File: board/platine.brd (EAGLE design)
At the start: 100 x 80 mm, 33 parts, among them IC2 SPS-1, T1 BC846, T2 BC846, X11 22-23-2031, X15 22-23-2031, X16 22-23-2031, X17 22-23-2031, X18 22-23-2031, X3 1751251, X4 1751251, X5 1751251, X7 1751248, X8 1751248, X9 1751248

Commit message: New board
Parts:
- added C10, C2, C3, C4, C5, C6, C7, C8, C9: (no value), rcl:C1206
- added L1, L2, L3, L4: (no value), rcl:R0402
- added R8: 220K, rcl:R0603
- C1: device rcl:C1206 -> rcl:C0603
- R1: value 10k -> 1K; device rcl:M1206 -> rcl:R0603
- R2, R3, R5, R6, R7: device rcl:M1206 -> rcl:R0603
- R4: value 3k -> 1K; device rcl:M1206 -> rcl:R0603
- moved X18 34.9 mm to (61.4, 49.2), turned to 90 degrees
- moved R6 32.0 mm to (40.0, 39.1), turned to 180 degrees
- moved R7 30.7 mm to (41.9, 36.6)
- moved SV1 29.2 mm to (40.7, 5.23)
- moved R5 27.9 mm to (39.1, 36.1), turned to 270 degrees
- moved C1 27.3 mm to (31.3, 34.0)
- moved X15 26.3 mm to (52.5, 38.8), turned to 90 degrees
- moved R2 18.9 mm to (35.7, 54.2), turned to 270 degrees
- moved R4 17.7 mm to (41.2, 54.8), turned to 90 degrees
- moved X17 12.9 mm to (52.6, 49.2), turned to 90 degrees
- moved R3 10.8 mm to (36.5, 57.3), turned to 180 degrees
- moved U$1 10.4 mm to (31.6, 43.5), turned to 90 degrees
- moved X16 9.46 mm to (61.4, 38.8), turned to 90 degrees
- moved R1 8.71 mm to (35.7, 60.7), turned to 90 degrees
- moved T2 6.54 mm to (40.2, 60.5)
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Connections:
- removed net N$25: F3.2A, X10.1, X11.1
- new net N$46: L3.1, SV1.21
- new net N$47: L4.2, R6.1, R7.2
- net +24V: now also C4.2, C6.2, C7.2, C9.2
- net +5V: now also C2.2, C5.2, F3.2A, X10.1, X11.1
- net GND: now also C10.1, C2.1, C3.1, C4.1, C5.1, C6.1, C7.1, C8.1, C9.1, R8.1, SV1.14, SV1.20, SV1.25, SV1.6, SV1.9, X11.3, X2.8, X2.9, X3.1, X3.2, X4.2, X4.3, X5.2, X5.3, X7.1, X8.2, X9.2
- net N$22: now also L2.2; no longer SV1.23
- net N$23: now also L3.2; no longer SV1.19
- net N$3: now also R8.2
- net N$41: now also C3.2
- net N$42: now also L1.1, SV1.24; no longer X3.1, X3.2, X4.2, X4.3, X5.2, X5.3
- net N$44: now also C10.2, C8.2, F2.2A, X9.1
- net N$45: now also L2.1, SV1.23; no longer X7.1, X8.2, X9.2
- net N$5: now also L1.2; no longer SV1.5
- net N$6: now also L4.1, SV1.19; no longer R6.1, R7.2, SV1.21
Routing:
- net GND: track 0.00 -> 641.3 mm, vias 0 -> 2
- net +5V: track 0.00 -> 277.5 mm, vias 0 -> 6
- net +24V: track 0.00 -> 247.9 mm, vias 0 -> 3
- net N$30: track 0.00 -> 74.0 mm, vias 0 -> 2
- net N$6: track 0.00 -> 52.6 mm, vias 0 -> 1
- net N$10: track 0.00 -> 52.1 mm, vias 0 -> 1
- net N$39: track 0.00 -> 46.7 mm
- net N$38: track 0.00 -> 46.6 mm
- net N$37: track 0.00 -> 45.6 mm
- net N$44: track 0.00 -> 44.9 mm
- net N$19: track 0.00 -> 44.3 mm
- net N$18: track 0.00 -> 43.5 mm, vias 0 -> 1
- net N$17: track 0.00 -> 41.6 mm, vias 0 -> 1
- net N$28: track 0.00 -> 40.8 mm, vias 0 -> 1
- net N$14: track 0.00 -> 40.3 mm
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- added copper zone on layer 1, net GND
- added copper zone on layer 16, net GND

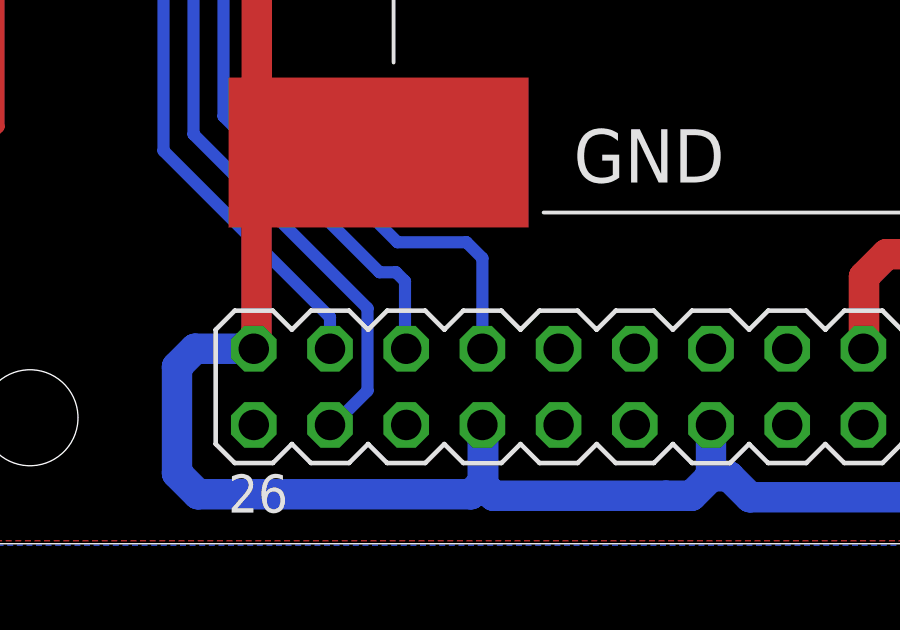
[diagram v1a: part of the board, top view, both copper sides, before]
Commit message: fix(board): switch MISO and MOSI
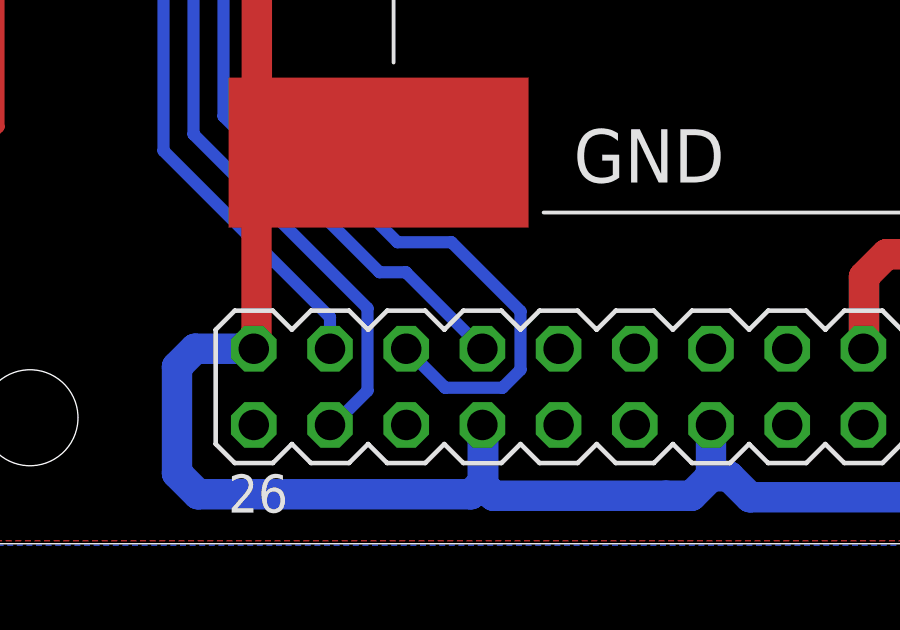
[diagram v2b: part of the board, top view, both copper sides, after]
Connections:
- net N$46: now also SV1.19; no longer SV1.21
- net N$6: now also SV1.21; no longer SV1.19
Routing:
- net N$6: track 52.6 -> 58.1 mm
- net N$46: track 24.4 -> 25.6 mm
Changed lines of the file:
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@@
 <?xml version="1.0" encoding="utf-8"?>
 <!DOCTYPE eagle SYSTEM "eagle.dtd">
-<eagle version="6.3">
+<eagle version="6.4">
 <drawing>
 <settings>
@@
 <signal name="N$6">
 <contactref element="L4" pad="1"/>
-<contactref element="SV1" pad="19"/>
 <wire x1="44.44" y1="34.64" x2="44.83" y2="34.25" width="0.4064" layer="1"/>
 <wire x1="44.83" y1="34.25" x2="46" y2="34.25" width="0.4064" layer="1"/>
@@
 <wire x1="25.6" y1="31.25" x2="25.6" y2="14.7" width="0.4064" layer="16"/>
 <wire x1="25.6" y1="14.7" x2="30.25" y2="10.05" width="0.4064" layer="16"/>
-<wire x1="30.25" y1="10.05" x2="32.55" y2="10.05" width="0.4064" layer="16"/>
-<wire x1="32.55" y1="10.05" x2="33.08" y2="9.52" width="0.4064" layer="16"/>
-<wire x1="33.08" y1="9.52" x2="33.08" y2="6.5" width="0.4064" layer="16"/>
+<contactref element="SV1" pad="21"/>
+<wire x1="32.05" y1="10.05" x2="34.35" y2="7.75" width="0.4064" layer="16"/>
+<wire x1="34.35" y1="7.75" x2="34.35" y2="5.8" width="0.4064" layer="16"/>
+<wire x1="34.35" y1="5.8" x2="33.75" y2="5.2" width="0.4064" layer="16"/>
+<wire x1="33.75" y1="5.2" x2="31.84" y2="5.2" width="0.4064" layer="16"/>
+<wire x1="31.84" y1="5.2" x2="30.54" y2="6.5" width="0.4064" layer="16"/>
+<wire x1="30.25" y1="10.05" x2="32.05" y2="10.05" width="0.4064" layer="16"/>
 </signal>
 <signal name="N$26">
@@
 <signal name="N$46">
 <contactref element="L3" pad="1"/>
-<contactref element="SV1" pad="21"/>
-<wire x1="30.54" y1="6.5" x2="30.5" y2="6.54" width="0.4064" layer="16"/>
-<wire x1="30.5" y1="6.54" x2="30.5" y2="8.75" width="0.4064" layer="16"/>
-<wire x1="30.5" y1="8.75" x2="30.2" y2="9.05" width="0.4064" layer="16"/>
-<wire x1="30.2" y1="9.05" x2="29.65" y2="9.05" width="0.4064" layer="16"/>
+<wire x1="30.53" y1="9.05" x2="29.65" y2="9.05" width="0.4064" layer="16"/>
 <wire x1="29.65" y1="9.05" x2="24.45" y2="14.25" width="0.4064" layer="16"/>
 <wire x1="24.45" y1="14.25" x2="24.45" y2="21.2" width="0.4064" layer="16"/>
@@
 <wire x1="20.25" y1="22.9" x2="20.23" y2="22.92" width="0.4064" layer="1"/>
 <wire x1="20.23" y1="22.92" x2="20.23" y2="24.84" width="0.4064" layer="1"/>
+<contactref element="SV1" pad="19"/>
+<wire x1="30.53" y1="9.05" x2="33.08" y2="6.5" width="0.4064" layer="16"/>
 </signal>
 <signal name="N$47">

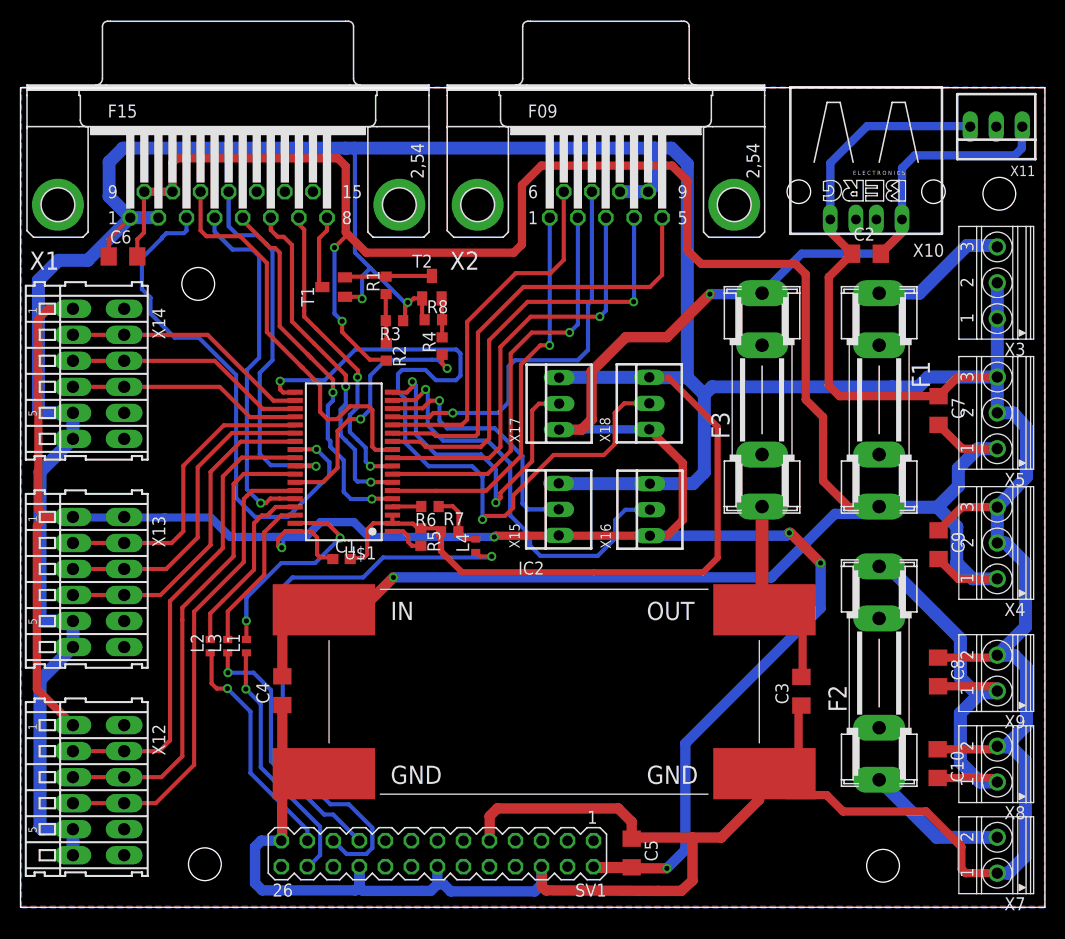
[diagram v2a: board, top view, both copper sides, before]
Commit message: Replaced wrong transistor
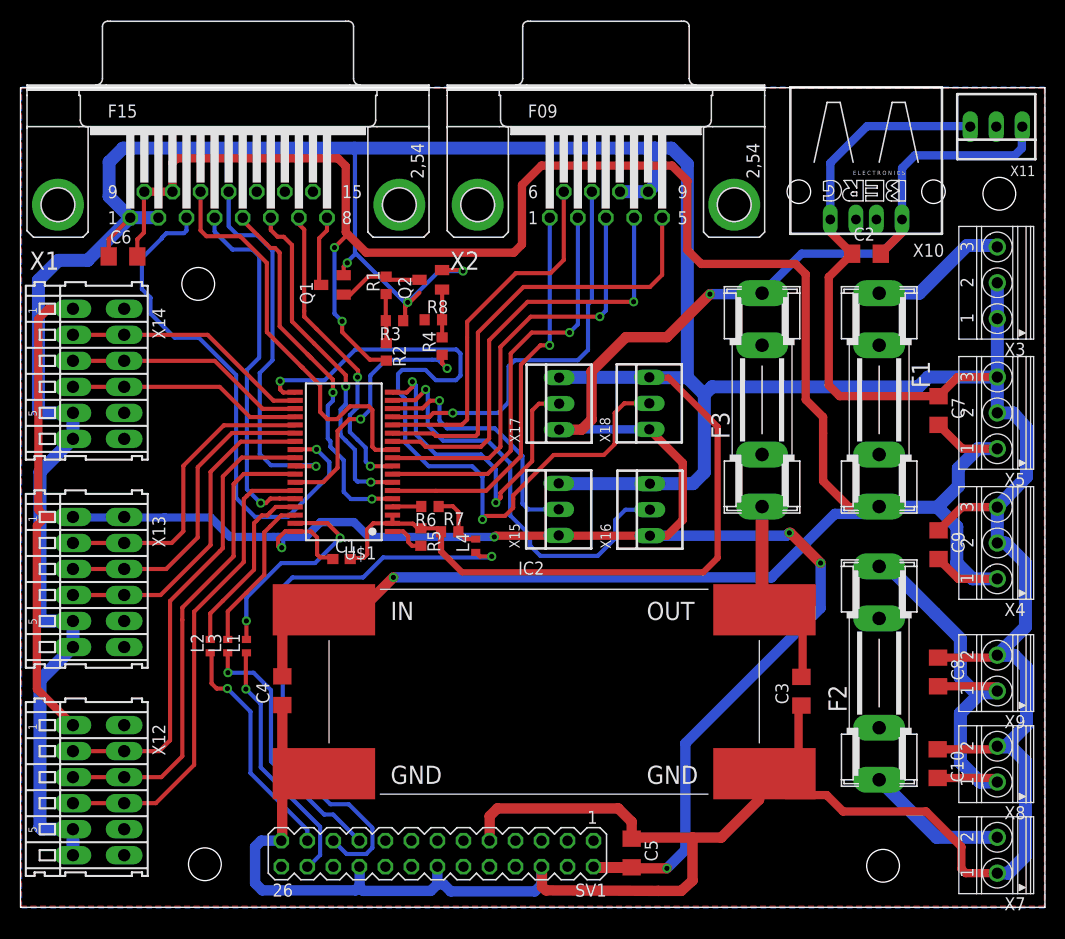
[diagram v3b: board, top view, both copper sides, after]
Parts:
- removed T1, T2: BC846, transistor:SOT23-EBC
- added Q1, Q2: (no value), semicon-smd-ipc:SOT23
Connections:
- net GND: now also Q1.2, Q2.2; no longer T1.E, T2.E
- net N$2: now also Q1.1, Q2.3; no longer T1.B, T2.C
- net N$3: now also Q2.1; no longer T2.B
- net N$7: now also Q1.3; no longer T1.C
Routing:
- net GND: track 641.3 -> 644.2 mm, vias 2 -> 3
- net N$3: track 3.83 -> 4.69 mm
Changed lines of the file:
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@@
 <?xml version="1.0" encoding="utf-8"?>
 <!DOCTYPE eagle SYSTEM "eagle.dtd">
-<eagle version="6.4">
+<eagle version="6.5.0">
 <drawing>
 <settings>
@@
 </autorouter>
 <elements>
-<element name="T1" library="transistor" package="SOT23-EBC" value="BC846" x="30.57" y="60.54" rot="R90"/>
-<element name="T2" library="transistor" package="SOT23-EBC" value="BC846" x="40.16" y="60.53"/>
 <element name="R1" library="rcl" package="R0603" value="1K" x="35.69" y="60.71" rot="R90"/>
 <element name="R2" library="rcl" package="R0603" value="21k" x="35.71" y="54.21" rot="R270"/>
@@
 <element name="C10" library="rcl" package="C1206" value="" x="89.53" y="14.02" rot="R270"/>
 <element name="R8" library="rcl" package="R0603" value="220K" x="40.3" y="57.35"/>
+<element name="Q1" library="semicon-smd-ipc" package="SOT23" value="" x="30.45" y="60.75" rot="R90"/>
+<element name="Q2" library="semicon-smd-ipc" package="SOT23" value="" x="40.05" y="61.25" rot="R90"/>
 </elements>
 <signals>
 <signal name="N$3">
-<contactref element="T2" pad="B"/>
 <contactref element="R4" pad="2"/>
 <contactref element="R8" pad="2"/>
-<wire x1="41.11" y1="59.43" x2="41.16" y2="59.38" width="0.4064" layer="1"/>
 <wire x1="41.16" y1="55.63" x2="41.16" y2="57.34" width="0.4064" layer="1"/>
 <wire x1="41.16" y1="57.34" x2="41.15" y2="57.35" width="0.4064" layer="1"/>
-<wire x1="41.16" y1="59.38" x2="41.16" y2="57.36" width="0.4064" layer="1"/>
+<wire x1="41.16" y1="60.3" x2="41.16" y2="57.36" width="0.4064" layer="1"/>
 <wire x1="41.16" y1="57.36" x2="41.15" y2="57.35" width="0.4064" layer="1"/>
+<contactref element="Q2" pad="1"/>
+<wire x1="41.15" y1="60.3" x2="41.16" y2="60.3" width="0.4064" layer="1"/>
 </signal>
 <signal name="GND">
-<contactref element="T1" pad="E"/>
-<contactref element="T2" pad="E"/>
 <contactref element="R3" pad="1"/>
 <contactref element="R5" pad="1"/>
@@
 <wire x1="37.36" y1="57.26" x2="37.55" y2="57.45" width="0.4064" layer="1"/>
 <wire x1="37.55" y1="57.45" x2="37.55" y2="58.6" width="0.4064" layer="1"/>
-<wire x1="37.55" y1="58.6" x2="38.38" y2="59.43" width="0.4064" layer="1"/>
-<wire x1="38.38" y1="59.43" x2="39.21" y2="59.43" width="0.4064" layer="1"/>
+<wire x1="37.55" y1="58.6" x2="38.95" y2="60" width="0.4064" layer="1"/>
 <wire x1="52.58" y1="51.7" x2="52.61" y2="51.73" width="1.27" layer="16"/>
 <wire x1="52.61" y1="51.73" x2="61.38" y2="51.73" width="1.27" layer="16"/>
@@
 <wire x1="52.57" y1="41.35" x2="61.44" y2="41.35" width="1.27" layer="16"/>
 <wire x1="66.75" y1="50.05" x2="67.5" y2="50.8" width="1.27" layer="16"/>
-<wire x1="67.5" y1="50.8" x2="85.1" y2="50.8" width="1.27" layer="16"/>
-<wire x1="85.1" y1="50.8" x2="87.65" y2="50.8" width="1.27" layer="16"/>
+<wire x1="67.5" y1="50.8" x2="87.65" y2="50.8" width="1.27" layer="16"/>
 <wire x1="87.65" y1="50.8" x2="88.61" y2="51.76" width="1.27" layer="16"/>
 <wire x1="88.61" y1="51.76" x2="95.35" y2="51.76" width="1.27" layer="16"/>
@@
 <wire x1="8.65" y1="69.3788" x2="8.65" y2="72.75" width="1.27" layer="16"/>
 <wire x1="8.65" y1="72.75" x2="10" y2="74.1" width="1.27" layer="16"/>
-<wire x1="10" y1="74.1" x2="31.75" y2="74.1" width="1.27" layer="16"/>
-<wire x1="31.75" y1="74.1" x2="32.6" y2="74.1" width="1.27" layer="16"/>
+<wire x1="10" y1="74.1" x2="32.6" y2="74.1" width="1.27" layer="16"/>
 <wire x1="32.6" y1="74.1" x2="61.9" y2="74.1" width="1.27" layer="16"/>
 <wire x1="61.9" y1="74.1" x2="63.55" y2="74.1" width="1.27" layer="16"/>
@@
 <wire x1="92.27" y1="3.33" x2="95.35" y2="3.33" width="0.8128" layer="1"/>
 <wire x1="8.61" y1="63.53" x2="8.61" y2="65.2012" width="0.4064" layer="1"/>
-<wire x1="8.61" y1="65.2012" x2="10.2544" y2="66.8456" width="0.4064" layer="1"/>
-<wire x1="10.2544" y1="66.8456" x2="10.7188" y2="67.31" width="0.4064" layer="1"/>
-<wire x1="39.21" y1="59.43" x2="39.21" y2="57.59" width="0.4064" layer="1"/>
+<wire x1="8.61" y1="65.2012" x2="10.7188" y2="67.31" width="0.4064" layer="1"/>
 <wire x1="39.21" y1="57.59" x2="39.45" y2="57.35" width="0.4064" layer="1"/>
 <wire x1="37.55" y1="58.6" x2="37.55" y2="58.8" width="0.4064" layer="1"/>
@@
 <via x="37.8" y="59.05" extent="1-16" drill="0.5"/>
 <wire x1="37.8" y1="59.05" x2="37.5" y2="59.05" width="0.4064" layer="16"/>
-<wire x1="37.5" y1="59.05" x2="34.15" y2="62.4" width="0.4064" layer="16"/>
-<wire x1="34.15" y1="62.4" x2="32.65" y2="63.9" width="0.4064" layer="16"/>
+<wire x1="37.5" y1="59.05" x2="32.725" y2="63.825" width="0.4064" layer="16"/>
+<wire x1="32.725" y1="63.825" x2="32.65" y2="63.9" width="0.4064" layer="16"/>
 <wire x1="32.65" y1="63.9" x2="32.65" y2="74.05" width="0.4064" layer="16"/>
 <wire x1="32.65" y1="74.05" x2="32.6" y2="74.1" width="0.4064" layer="16"/>
-<wire x1="31.67" y1="59.59" x2="33.16" y2="59.59" width="0.4064" layer="1"/>
-<wire x1="33.16" y1="59.59" x2="33.35" y2="59.4" width="0.4064" layer="1"/>
-<via x="33.35" y="59.4" extent="1-16" drill="0.5"/>
-<wire x1="33.35" y1="59.4" x2="33.35" y2="61.6" width="0.4064" layer="16"/>
-<wire x1="33.35" y1="61.6" x2="34.15" y2="62.4" width="0.4064" layer="16"/>
 <wire x1="25.56" y1="19.74" x2="25.56" y2="13.44" width="1.016" layer="1"/>
 <wire x1="25.56" y1="13.44" x2="26" y2="13" width="1.016" layer="1"/>
@@
 <wire x1="41.05" y1="36.65" x2="41.05" y2="34.75" width="0.6096" layer="1"/>
 <wire x1="41.05" y1="34.75" x2="43.1" y2="32.7" width="0.6096" layer="1"/>
-<wire x1="43.1" y1="32.7" x2="56" y2="32.7" width="0.6096" layer="1"/>
-<wire x1="56" y1="32.7" x2="66.65" y2="32.7" width="0.6096" layer="1"/>
+<wire x1="43.1" y1="32.7" x2="66.65" y2="32.7" width="0.6096" layer="1"/>
 <wire x1="66.65" y1="32.7" x2="68.05" y2="34.1" width="0.6096" layer="1"/>
 <wire x1="68.05" y1="34.1" x2="68.05" y2="46.9" width="0.6096" layer="1"/>
@@
 <wire x1="25.55" y1="12.25" x2="26" y2="12.7" width="1.016" layer="1"/>
 <wire x1="26" y1="12.7" x2="26" y2="13" width="1.016" layer="1"/>
-<wire x1="33.08" y1="3.96" x2="33.1" y2="3.94" width="1.016" layer="16"/>
-<wire x1="33.1" y1="3.94" x2="33.1" y2="2.05" width="1.016" layer="16"/>
 <wire x1="33.1" y1="2.05" x2="33.1" y2="1.95" width="1.016" layer="16"/>
 <wire x1="33.1" y1="1.95" x2="33.45" y2="1.6" width="1.016" layer="16"/>
-<wire x1="33.45" y1="1.6" x2="39.2" y2="1.6" width="1.016" layer="16"/>
-<wire x1="39.2" y1="1.6" x2="40.05" y2="1.6" width="1.016" layer="16"/>
+<wire x1="33.45" y1="1.6" x2="40.05" y2="1.6" width="1.016" layer="16"/>
 <wire x1="40.05" y1="1.6" x2="40.7" y2="2.25" width="1.016" layer="16"/>
 <wire x1="40.7" y1="2.25" x2="40.7" y2="3.96" width="1.016" layer="16"/>
@@
 <vertex x="0.05" y="0.1"/>
 </polygon>
+<contactref element="Q1" pad="2"/>
+<contactref element="Q2" pad="2"/>
+<wire x1="41.15" y1="62.2" x2="40.75" y2="62.2" width="0.4064" layer="1"/>
+<wire x1="31.55" y1="61.7" x2="31.55" y2="62.55" width="0.4064" layer="1"/>
+<wire x1="31.55" y1="62.55" x2="31.9" y2="62.9" width="0.4064" layer="1"/>
+<via x="31.9" y="62.9" extent="1-16" drill="0.5"/>
+<wire x1="31.9" y1="62.9" x2="31.9" y2="63" width="0.4064" layer="16"/>
+<wire x1="31.9" y1="63" x2="32.725" y2="63.825" width="0.4064" layer="16"/>
+<wire x1="41.15" y1="62.2" x2="43.1" y2="62.2" width="0.4064" layer="1"/>
+<wire x1="43.1" y1="62.2" x2="43.2" y2="62.1" width="0.4064" layer="1"/>
+<via x="43.2" y="62.1" extent="1-16" drill="0.5"/>
+<wire x1="43.2" y1="62.1" x2="40.85" y2="62.1" width="0.4064" layer="16"/>
+<wire x1="40.85" y1="62.1" x2="37.8" y2="59.05" width="0.4064" layer="16"/>
 </signal>
 <signal name="+24V">
@@
 <signal name="N$2">
 <contactref element="R1" pad="2"/>
-<contactref element="T2" pad="C"/>
-<contactref element="T1" pad="B"/>
-<wire x1="31.67" y1="61.49" x2="31.74" y2="61.56" width="0.4064" layer="1"/>
-<wire x1="31.74" y1="61.56" x2="35.69" y2="61.56" width="0.4064" layer="1"/>
+<wire x1="33.95" y1="61.56" x2="35.69" y2="61.56" width="0.4064" layer="1"/>
 <wire x1="35.69" y1="61.56" x2="35.76" y2="61.63" width="0.4064" layer="1"/>
-<wire x1="35.76" y1="61.63" x2="40.16" y2="61.63" width="0.4064" layer="1"/>
+<contactref element="Q1" pad="1"/>
+<contactref element="Q2" pad="3"/>
+<wire x1="38.95" y1="61.25" x2="36" y2="61.25" width="0.4064" layer="1"/>
+<wire x1="36" y1="61.25" x2="35.69" y2="61.56" width="0.4064" layer="1"/>
+<wire x1="31.55" y1="59.8" x2="32.19" y2="59.8" width="0.4064" layer="1"/>
+<wire x1="32.19" y1="59.8" x2="33.95" y2="61.56" width="0.4064" layer="1"/>
 </signal>
 <signal name="N$7">
-<contactref element="T1" pad="C"/>
 <contactref element="X1" pad="8"/>
-<wire x1="29.47" y1="60.54" x2="29.15" y2="60.86" width="0.4064" layer="1"/>
 <wire x1="29.15" y1="60.86" x2="29.15" y2="65.3" width="0.4064" layer="1"/>
 <wire x1="29.15" y1="65.3" x2="29.9212" y2="66.0712" width="0.4064" layer="1"/>
 <wire x1="29.9212" y1="66.0712" x2="29.9212" y2="67.31" width="0.4064" layer="1"/>
+<contactref element="Q1" pad="3"/>
+<wire x1="29.35" y1="60.75" x2="29.26" y2="60.75" width="0.4064" layer="1"/>
+<wire x1="29.26" y1="60.75" x2="29.15" y2="60.86" width="0.4064" layer="1"/>
 </signal>
 <signal name="N$8">
